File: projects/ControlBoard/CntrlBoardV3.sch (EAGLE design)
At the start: 105 parts, among them J7 M83-LMT1M2N36, J8 M80-5101005, J9 M50-3600542, M1 AON7522E, M2 SI4427BDY-T1-E3CT-ND, U1 MR25H40MDF, U10 LT6015, U11 LT6016, U2 M24M02-DR, U3 SN74LVC1G125, U4 SN74LVC1G125, U6 MR25H40MDF, U7 AD7991-1, U8 LTC1380-GN, U9 LTC1380-GN

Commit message: Finished control board schematic. Completed preliminary component layout and board dimensions. Also includes library updates to support added components and connectors.
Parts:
- removed U$5: TPS63002, CNTRL_BOARD:TPS6300X
- added D3, D4: MSP5.0A, BrownSpaceEngineering:TVSMSP
- added D5: MSP3V3, BrownSpaceEngineering:TVSMSP
- added J1, J2, J3, J5: HARWIN_06, CNTRL_BOARD:HARWIN_06
- added J4: M80-54010, BrownSpaceEngineering:M80-54010
- added J6: M80-54020, BrownSpaceEngineering:M80-54020
- added R46, R47, R49: 10K, BrownSpaceEngineering:RES0805
- added R48: 21K, BrownSpaceEngineering:RES0805
- added R50, R51: 0R, BrownSpaceEngineering:RES1210
- added U13: TPS63002, CNTRL_BOARD:TPS6300X
- renumbered U$2 to U14, U$3 to U15, U$4 to U12
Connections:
- net N$29 renamed L1_RUN_CHG
- net N$30 renamed L2_RUN_CHG
- net N$31 renamed L1_DISG
- net N$32 renamed L2_DISG
- removed net LED_SDHN: U5.OUT
- removed net LIFE_B1_OUTEN: UC1.PA00
- new net !BATT_INT!: UC1.PA04
- new net ANT_DRV1: J6.P$9, UC1.PA13
- new net ANT_DRV2: J6.P$10, UC1.PA14
- new net ANT_DRV3: J6.P$11, UC1.PA15
- new net DET_RTN: J6.P$7, UC1.PB14
- new net L1_CHGN: J7.P$30
- new net L1_FAULTN: J7.P$29
- new net L1_REF: J7.P$11
- new net L2_CHGN: J7.P$32
- new net L2_FAULTN: J7.P$31
- new net L2_REF: J7.P$12
- new net LED1SNS: J6.P$12, UC1.PA28
- new net LED2SNS: J6.P$13, UC1.PA27
- new net LED3SNS: J6.P$14, UC1.PB23
- new net LED4SNS: J6.P$15, UC1.PB22
- new net LED_SHDN: J6.P$5, U5.OUT
- new net LF1REF: J7.P$15, UC1.PB04
- new net LF2REF: J7.P$16, UC1.PB05
- new net LFB1OSNS: J7.P$13, UC1.PA11
- new net LFB1SNS: J7.P$14, UC1.PA10
- new net LFB2OSNS: J7.P$17, UC1.PA09
- new net LFB2SNS: J7.P$18, UC1.PA08
- new net LF_B1_OUTEN: J7.P$26, UC1.PA00
- new net LF_B1_RUNCHG: J7.P$25, UC1.PB03
- new net LF_B2_OUTEN: J7.P$28, UC1.PA01
- new net LF_B2_RUNCHG: J7.P$27, UC1.PB00, UC1.PB01
- new net LION1REF: UC1.PA02
- new net LION1_DISG: UC1.PB30
- new net LION2REF: UC1.PA03
- new net LION2_DISG: UC1.PB31
- new net LION2_RUN_CHG: UC1.PB02
- new net LION_OUT: J7.P$6
- new net VIN-EXT: D4.C, J4.P$1, R51.1
- new net VIN-INT: D3.C, J5.6, R50.2
- net !LED_CMD!: now also UC1.PA12
- net !RAD_SHDN!: now also UC1.PB17
- net !RESET!: now also J4.P$6
- net +3V3: now also D5.C, J4.P$10, J7.P$10, R46.1
- net +5V: now also J6.P$17, J7.P$5, R48.1, U13.FB, U13.VOUT; no longer U$5.FB, U$5.VOUT
- net 3V3REF: now also R46.2, R47.2
- net 5VREF: now also R48.2, R49.2
- net 5V_EN: now also U13.EN, UC1.PB11; no longer U$5.EN
- net GND: now also D3.A, D4.A, D5.A, J1.5, J2.5, J3.5, J4.P$9, J5.5, J6.P$16, J6.P$6, J7.P$7, R47.1, R49.1, U13.GND, U13.PGND; no longer U$5.GND, U$5.PGND
- net IRVDD: now also J1.4, J2.4, J3.4, J4.P$4, J5.4, J6.P$18
- net IR_PWR_CMD: now also UC1.PA22
- net L1_TEMP: now also U8.S3; no longer U8.S4
- net L2_TEMP: now also J7.P$2, U8.S2; no longer U8.S5
- net LED1TEMP: now also J6.P$1, U8.S7; no longer U8.S0
- net LED2TEMP: now also J6.P$2, U8.S6; no longer U8.S1
- net LED3TEMP: now also J6.P$3, U8.S5; no longer U8.S2
- net LED4TEMP: now also J6.P$4, U8.S4; no longer U8.S3
- net LF1_TEMP: now also J7.P$3, U8.S1; no longer U8.S6
- net LF3REF: now also UC1.PB06
- net LF3_TEMP: now also J7.P$4, U8.S0; no longer U8.S7
- net LF4REF: now also UC1.PB07
- net N$10: now also U13.PS/SYNC, U13.VINA; no longer U$5.PS/SYNC, U$5.VINA
- net N$7: now also U13.L1; no longer U$5.L1
- net N$8: now also U13.L2; no longer U$5.L2
- net PD_FLASH: now also J6.P$8
- net PD_OUT: now also UC1.PA07
- net PD_XN: now also J2.1
- net PD_XP: now also J5.1
- net PD_YN: now also J1.1
- net PD_ZN: now also J4.P$5
- net PD_ZP: now also J3.1
- net RAD_PWR_RUN: now also UC1.PB16
- net RX_DATA: now also UC1.PA25
- net RX_EN: now also UC1.PA21
- net SCL: now also J1.2, J2.2, J3.2, J4.P$2, J5.2, J6.P$20, J7.P$9
- net SDA: now also J1.3, J2.3, J3.3, J4.P$3, J5.3, J6.P$19, J7.P$8
- net SWDCLK: now also J4.P$7
- net SWDIO: now also J4.P$8
- net TEMP_OUT: now also UC1.PA06
- net TX_DATA: now also UC1.PA24
- net TX_EN: now also UC1.PA20
- net VIN: now also R50.1, R51.2, U13.VIN; no longer U$5.VIN
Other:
- note added: "+X Panel"
- note added: "+Z Panel"
- note added: "-X Panel"
- note added: "-Y Panel"
- note added: "-Z Panel (Umbilical Connector)"
- note added: "Driver Board"

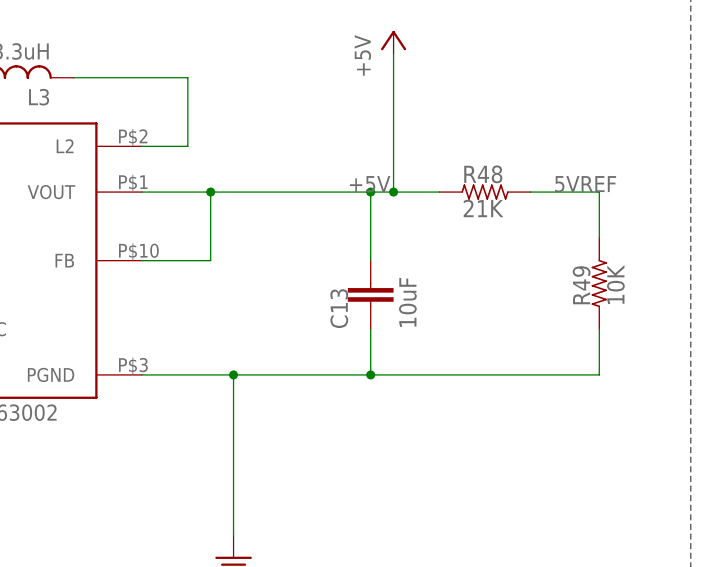
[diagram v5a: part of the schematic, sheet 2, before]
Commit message: Completed first round of cntrl board placement for all components.
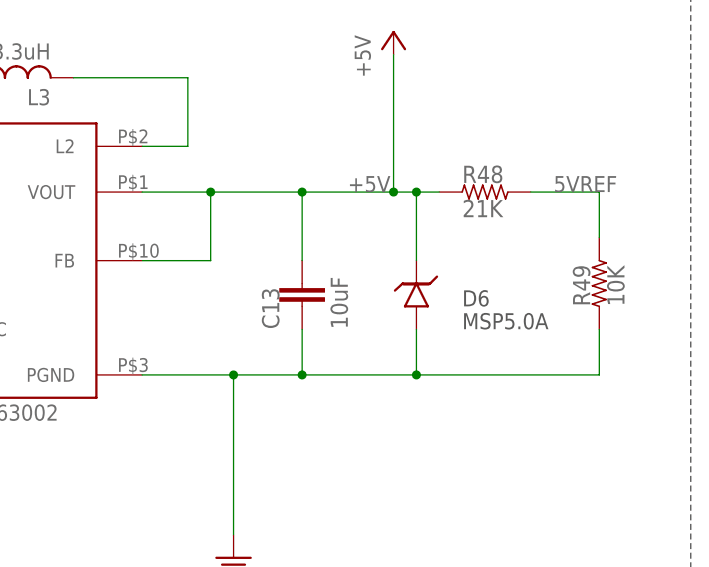
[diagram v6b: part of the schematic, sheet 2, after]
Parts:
- added D6: MSP5.0A, BrownSpaceEngineering:TVSMSP
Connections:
- net +5V: now also D6.C
- net GND: now also D6.A
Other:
- moved on the sheet: C13
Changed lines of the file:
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@@
 <part name="P+3" library="supply1" deviceset="+5V" device=""/>
 <part name="D5" library="BrownSpaceEngineering" deviceset="TVS" device="" technology="MSP" value="MSP3V3"/>
+<part name="D6" library="BrownSpaceEngineering" deviceset="TVS" device="" technology="MSP" value="MSP5.0A"/>
 </parts>
 <sheets>
@@
 <instance part="C11" gate="G$1" x="134.62" y="55.88"/>
 <instance part="C12" gate="G$1" x="63.5" y="50.8"/>
-<instance part="C13" gate="G$1" x="213.36" y="55.88"/>
+<instance part="C13" gate="G$1" x="205.74" y="55.88"/>
 <instance part="R9" gate="R$1" x="2.54" y="53.34" rot="R90"/>
 <instance part="R10" gate="R$1" x="147.32" y="60.96" rot="R90"/>
@@
 <instance part="R49" gate="R$1" x="238.76" y="58.42" rot="R90"/>
 <instance part="D5" gate="G$1" x="73.66" y="50.8"/>
+<instance part="D6" gate="G$1" x="218.44" y="55.88"/>
 </instances>
 <busses>
@@
 <pinref part="P+1" gate="1" pin="+5V"/>
 <wire x1="187.96" y1="68.58" x2="195.58" y2="68.58" width="0.1524" layer="91"/>
-<wire x1="195.58" y1="68.58" x2="213.36" y2="68.58" width="0.1524" layer="91"/>
-<wire x1="213.36" y1="68.58" x2="215.9" y2="68.58" width="0.1524" layer="91"/>
+<wire x1="195.58" y1="68.58" x2="205.74" y2="68.58" width="0.1524" layer="91"/>
+<wire x1="205.74" y1="68.58" x2="215.9" y2="68.58" width="0.1524" layer="91"/>
 <wire x1="215.9" y1="68.58" x2="215.9" y2="83.82" width="0.1524" layer="91"/>
 <label x="210.82" y="68.58" size="1.778" layer="95"/>
@@
 <junction x="195.58" y="68.58"/>
 <pinref part="C13" gate="G$1" pin="P$1"/>
-<wire x1="213.36" y1="60.96" x2="213.36" y2="68.58" width="0.1524" layer="91"/>
-<junction x="213.36" y="68.58"/>
+<wire x1="205.74" y1="60.96" x2="205.74" y2="68.58" width="0.1524" layer="91"/>
+<junction x="205.74" y="68.58"/>
 <pinref part="R48" gate="R$1" pin="1"/>
-<wire x1="220.98" y1="68.58" x2="215.9" y2="68.58" width="0.1524" layer="91"/>
+<wire x1="220.98" y1="68.58" x2="218.44" y2="68.58" width="0.1524" layer="91"/>
 <junction x="215.9" y="68.58"/>
+<pinref part="D6" gate="G$1" pin="C"/>
+<wire x1="218.44" y1="68.58" x2="215.9" y2="68.58" width="0.1524" layer="91"/>
+<wire x1="218.44" y1="60.96" x2="218.44" y2="68.58" width="0.1524" layer="91"/>
+<junction x="218.44" y="68.58"/>
 </segment>
 </net>
@@
 <wire x1="198.12" y1="48.26" x2="198.12" y2="30.48" width="0.1524" layer="91"/>
 <pinref part="C13" gate="G$1" pin="P$2"/>
-<wire x1="198.12" y1="48.26" x2="213.36" y2="48.26" width="0.1524" layer="91"/>
-<wire x1="213.36" y1="48.26" x2="213.36" y2="53.34" width="0.1524" layer="91"/>
+<wire x1="198.12" y1="48.26" x2="205.74" y2="48.26" width="0.1524" layer="91"/>
+<wire x1="205.74" y1="48.26" x2="205.74" y2="53.34" width="0.1524" layer="91"/>
 <junction x="198.12" y="48.26"/>
 <pinref part="R49" gate="R$1" pin="1"/>
-<wire x1="213.36" y1="48.26" x2="238.76" y2="48.26" width="0.1524" layer="91"/>
+<wire x1="205.74" y1="48.26" x2="218.44" y2="48.26" width="0.1524" layer="91"/>
+<wire x1="218.44" y1="48.26" x2="238.76" y2="48.26" width="0.1524" layer="91"/>
 <wire x1="238.76" y1="48.26" x2="238.76" y2="53.34" width="0.1524" layer="91"/>
-<junction x="213.36" y="48.26"/>
-</segment>
-</net>
+<junction x="205.74" y="48.26"/>
+<pinref part="D6" gate="G$1" pin="A"/>
+<wire x1="218.44" y1="53.34" x2="218.44" y2="48.26" width="0.1524" layer="91"/>
+<junction x="218.44" y="48.26"/>
+</segment>
+</net>

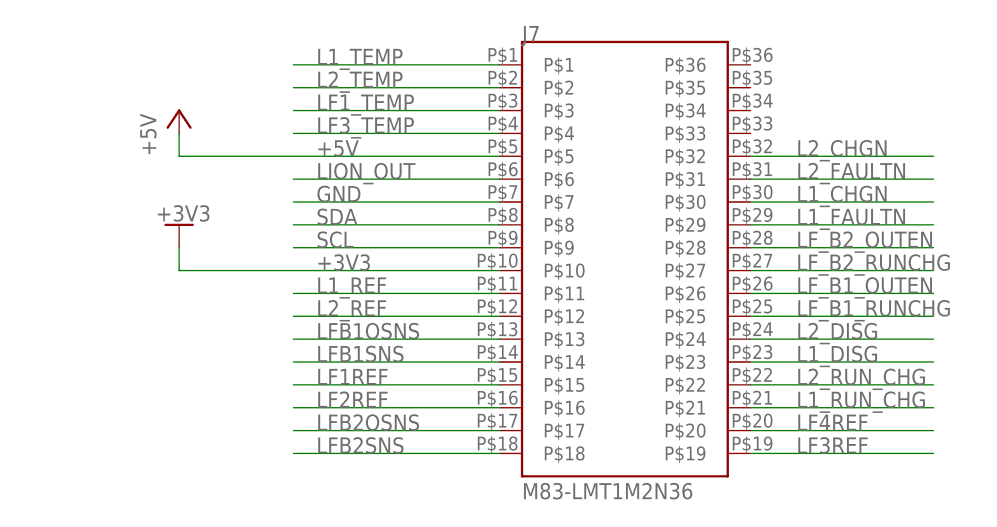
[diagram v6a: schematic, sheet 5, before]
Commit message: Continued work on Control Board layout - modification of some connector types and connector pinouts to optimize routing, initial power and ground routing.
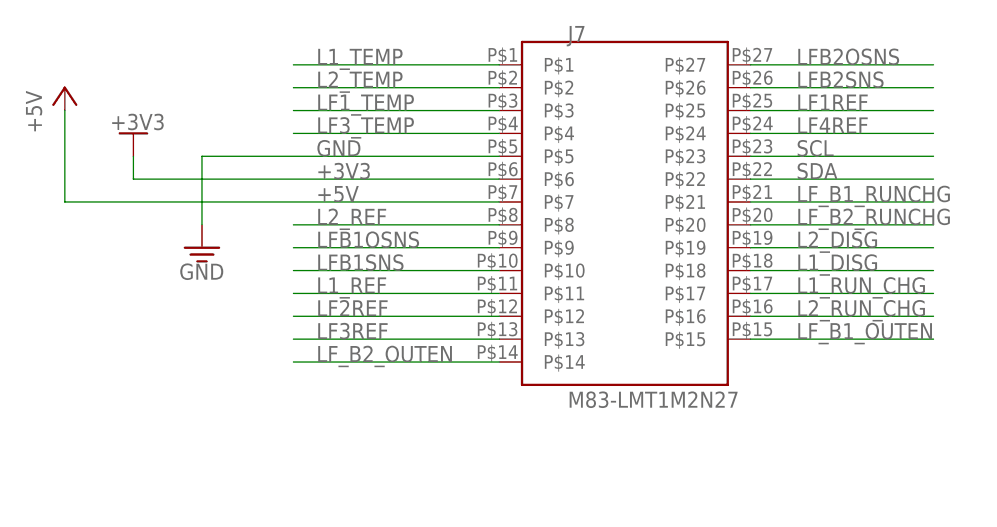
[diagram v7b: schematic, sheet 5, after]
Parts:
- added R52: 10M, BrownSpaceEngineering:RES0805
- J3: value HARWIN_06 -> M80-54006; device CNTRL_BOARD:HARWIN_06 -> BrownSpaceEngineering:M80-54006
- J5: value HARWIN_06 -> M80-54008; device CNTRL_BOARD:HARWIN_06 -> BrownSpaceEngineering:M80-54008
- J7: value M83-LMT1M2N36 -> M83-LMT1M2N27; device BrownSpaceEngineering:M83-LMT1M2N36 -> BrownSpaceEngineering:M83-LMT1M2N27
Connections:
- removed net !BATT_INT!: UC1.PA04
- removed net L1_CHGN: J7.P$30
- removed net L1_FAULTN: J7.P$29
- removed net L2_CHGN: J7.P$32
- removed net L2_FAULTN: J7.P$31
- removed net LION1REF: UC1.PA02
- removed net LION1_DISG: UC1.PB30
- removed net LION2REF: UC1.PA03
- removed net LION2_DISG: UC1.PB31
- removed net LION2_RUN_CHG: UC1.PB02
- removed net LION_OUT: J7.P$6
- net !CS2!: now also UC1.PB16; no longer UC1.PA23
- net !RAD_SHDN!: now also UC1.PA23; no longer UC1.PB17
- net +3V3: now also J7.P$6; no longer J7.P$10
- net +5V: now also J7.P$7; no longer J7.P$5
- net GND: now also J3.P$5, J5.P$5, J5.P$6, J7.P$5, R52.1; no longer J3.5, J5.5, J7.P$7
- net IRVDD: now also J3.P$4, J5.P$4; no longer J3.4, J5.4
- net IR_PWR_CMD: now also UC1.PB17; no longer UC1.PA22
- net L1_DISG: now also J7.P$18, UC1.PB30; no longer J7.P$23
- net L1_REF: now also UC1.PA07
- net L1_RUN_CHG: now also J7.P$17, UC1.PB00; no longer J7.P$21
- net L2_DISG: now also J7.P$19, UC1.PB31; no longer J7.P$24
- net L2_REF: now also J7.P$8, UC1.PA06; no longer J7.P$12
- net L2_RUN_CHG: now also J7.P$16, UC1.PB02; no longer J7.P$22
- net LF1REF: now also J7.P$25, UC1.PA05; no longer J7.P$15, UC1.PB04
- net LF2REF: now also J7.P$12, UC1.PA04; no longer J7.P$16, UC1.PB05
- net LF3REF: now also J7.P$13, UC1.PB07; no longer J7.P$19, UC1.PB06
- net LF4REF: now also J7.P$24, UC1.PB08; no longer J7.P$20, UC1.PB07
- net LFB1OSNS: now also J7.P$9; no longer J7.P$13
- net LFB1SNS: now also J7.P$10; no longer J7.P$14
- net LFB2OSNS: now also J7.P$27; no longer J7.P$17
- net LFB2SNS: now also J7.P$26; no longer J7.P$18
- net LF_B1_OUTEN: now also J7.P$15; no longer J7.P$26
- net LF_B1_RUNCHG: now also J7.P$21; no longer J7.P$25
- net LF_B2_OUTEN: now also J7.P$14; no longer J7.P$28
- net LF_B2_RUNCHG: now also J7.P$20; no longer J7.P$27, UC1.PB00
- net PD_OUT: now also UC1.PA02; no longer UC1.PA07
- net PD_XP: now also J5.P$1; no longer J5.1
- net PD_ZP: now also J3.P$1; no longer J3.1
- net RAD_PWR_RUN: now also UC1.PA22; no longer UC1.PB16
- net SCL: now also J3.P$3, J5.P$2, J7.P$23; no longer J3.2, J5.2, J7.P$9
- net SDA: now also J3.P$2, J5.P$3, J7.P$22; no longer J3.3, J5.3, J7.P$8
- net TEMP_OUT: now also UC1.PA03; no longer UC1.PA06
- net VIN: now also R52.2
- net VIN-INT: now also J5.P$7, J5.P$8; no longer J5.6
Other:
- note added: "CAREFUL: SOLAR PANEL PINOUTS ARE NOT THE SAME"
- note added: "D3 & D4 are TVS diodes with working voltage Vwr=5V"
- note added: "R52 Pulls Down Vin to GND for when both sources are disconnected."
- moved on the sheet: J3

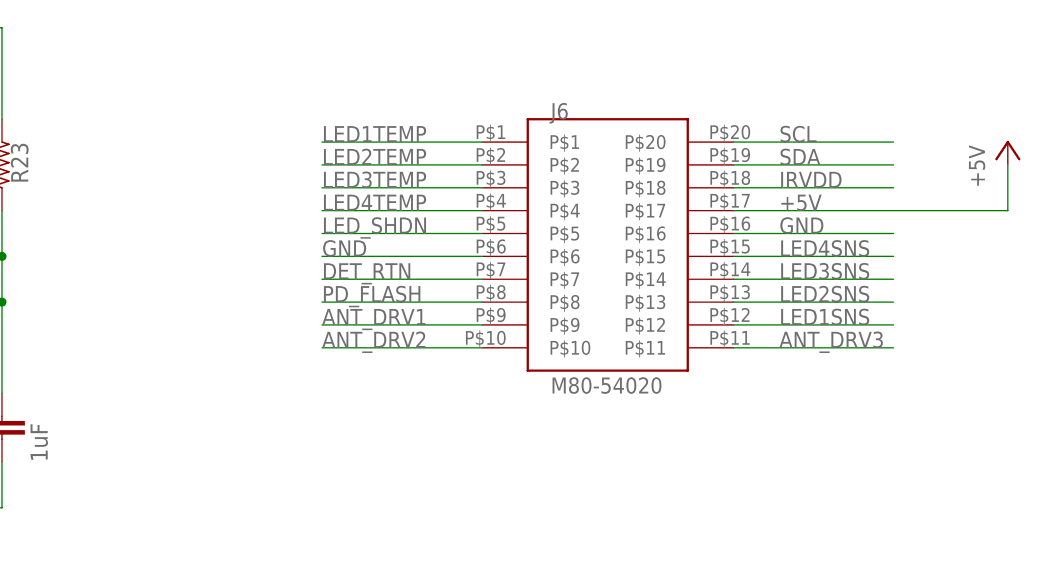
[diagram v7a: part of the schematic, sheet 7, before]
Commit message: Continued routing of Control Board.
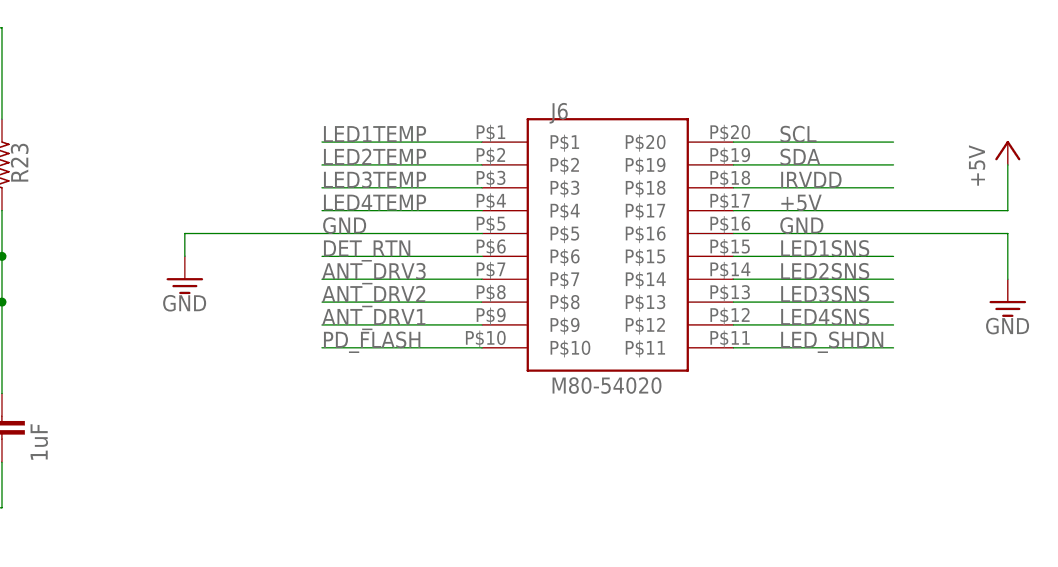
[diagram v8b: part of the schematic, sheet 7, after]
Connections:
- net !RAD_SHDN!: now also UC1.PA21; no longer UC1.PA23
- net !RESET!: now also J4.P$2; no longer J4.P$6
- net ANT_DRV2: now also J6.P$8; no longer J6.P$10
- net ANT_DRV3: now also J6.P$7; no longer J6.P$11
- net DET_RTN: now also J6.P$6; no longer J6.P$7
- net GND: now also J6.P$5; no longer J6.P$6
- net IRVDD: now also J4.P$6, J5.P$2; no longer J4.P$4, J5.P$4
- net LED1SNS: now also J6.P$15; no longer J6.P$12
- net LED2SNS: now also J6.P$14; no longer J6.P$13
- net LED3SNS: now also J6.P$13; no longer J6.P$14
- net LED4SNS: now also J6.P$12; no longer J6.P$15
- net LED_SHDN: now also J6.P$11; no longer J6.P$5
- net PD_FLASH: now also J6.P$10; no longer J6.P$8
- net RAD_PWR_RUN: now also UC1.PA20; no longer UC1.PA22
- net RX_EN: now also UC1.PA22; no longer UC1.PA21
- net SCL: now also J4.P$4, J5.P$4; no longer J4.P$2, J5.P$2
- net TX_EN: now also UC1.PA23; no longer UC1.PA20
